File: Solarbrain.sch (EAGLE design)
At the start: 50 parts, among them IC1 MCP73871, Q1 MOSFET-NCHANNELSMD, Q2 MOSFET-NCHANNELFDD8580, Q3 MOSFET-NCHANNELSMD, U1 ATMEGA128_SMD

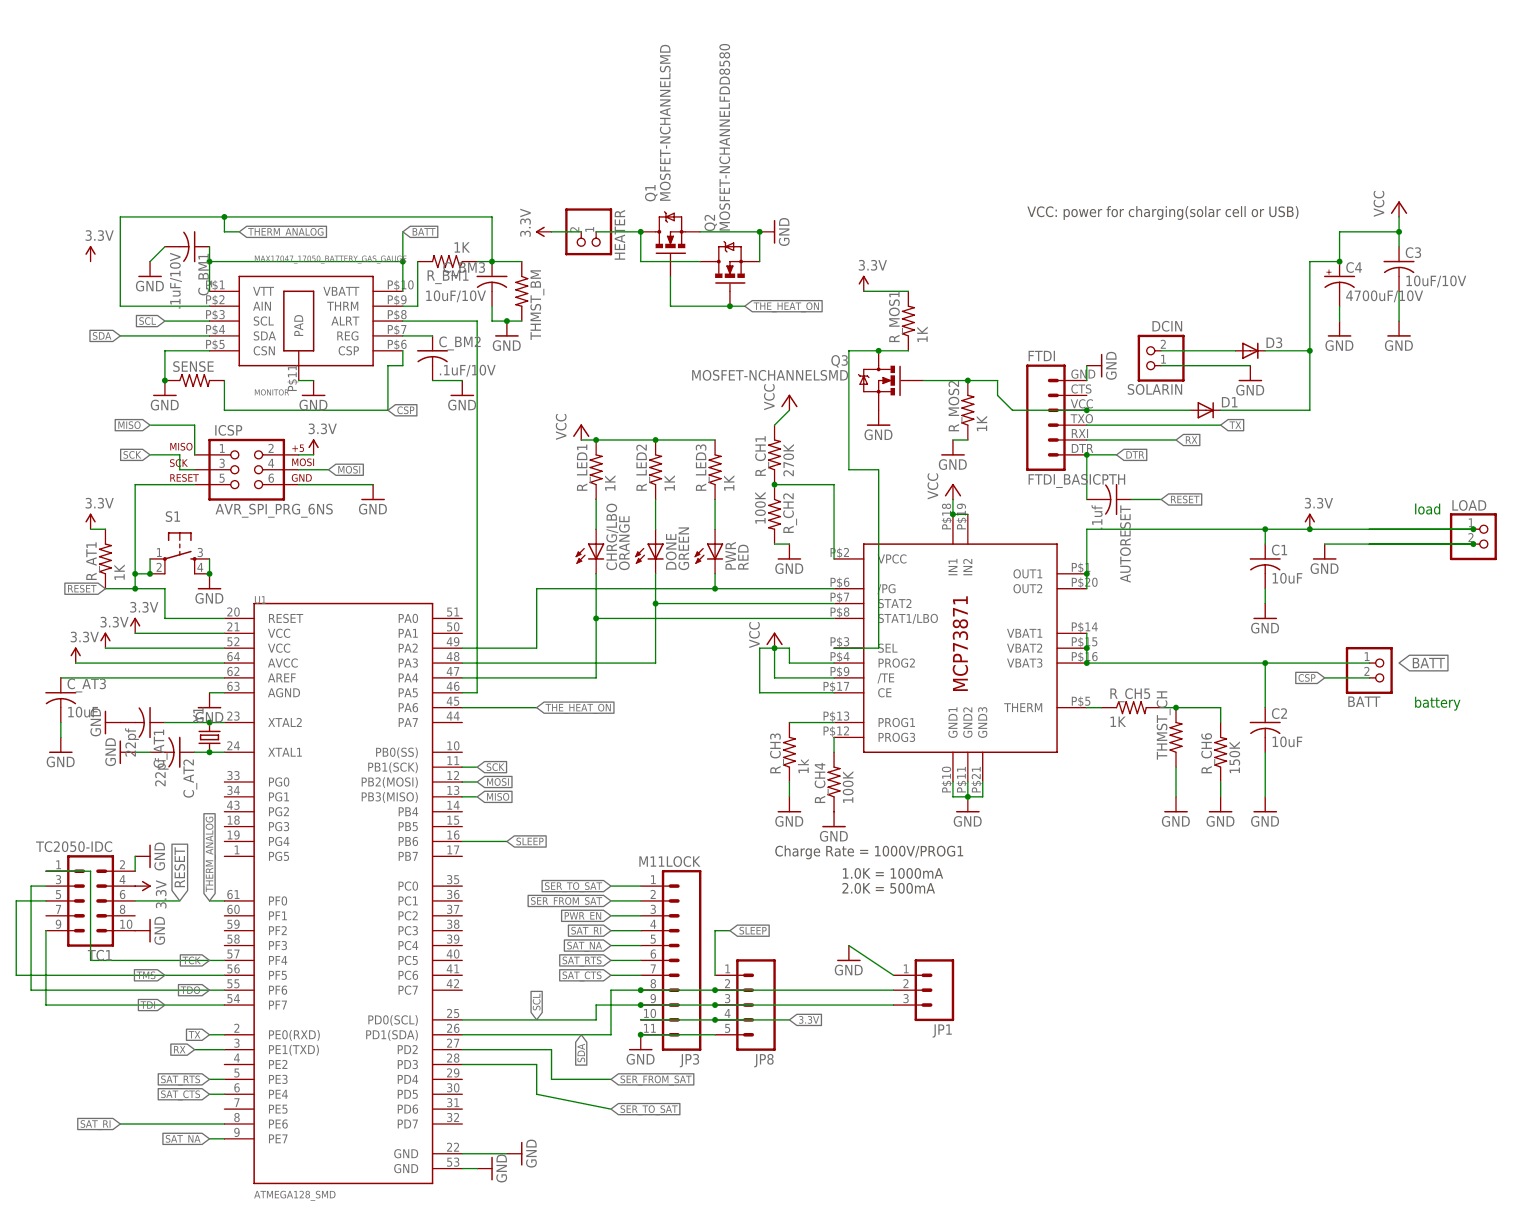
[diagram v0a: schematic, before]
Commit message: fixed a broken connection, clarification on schematic
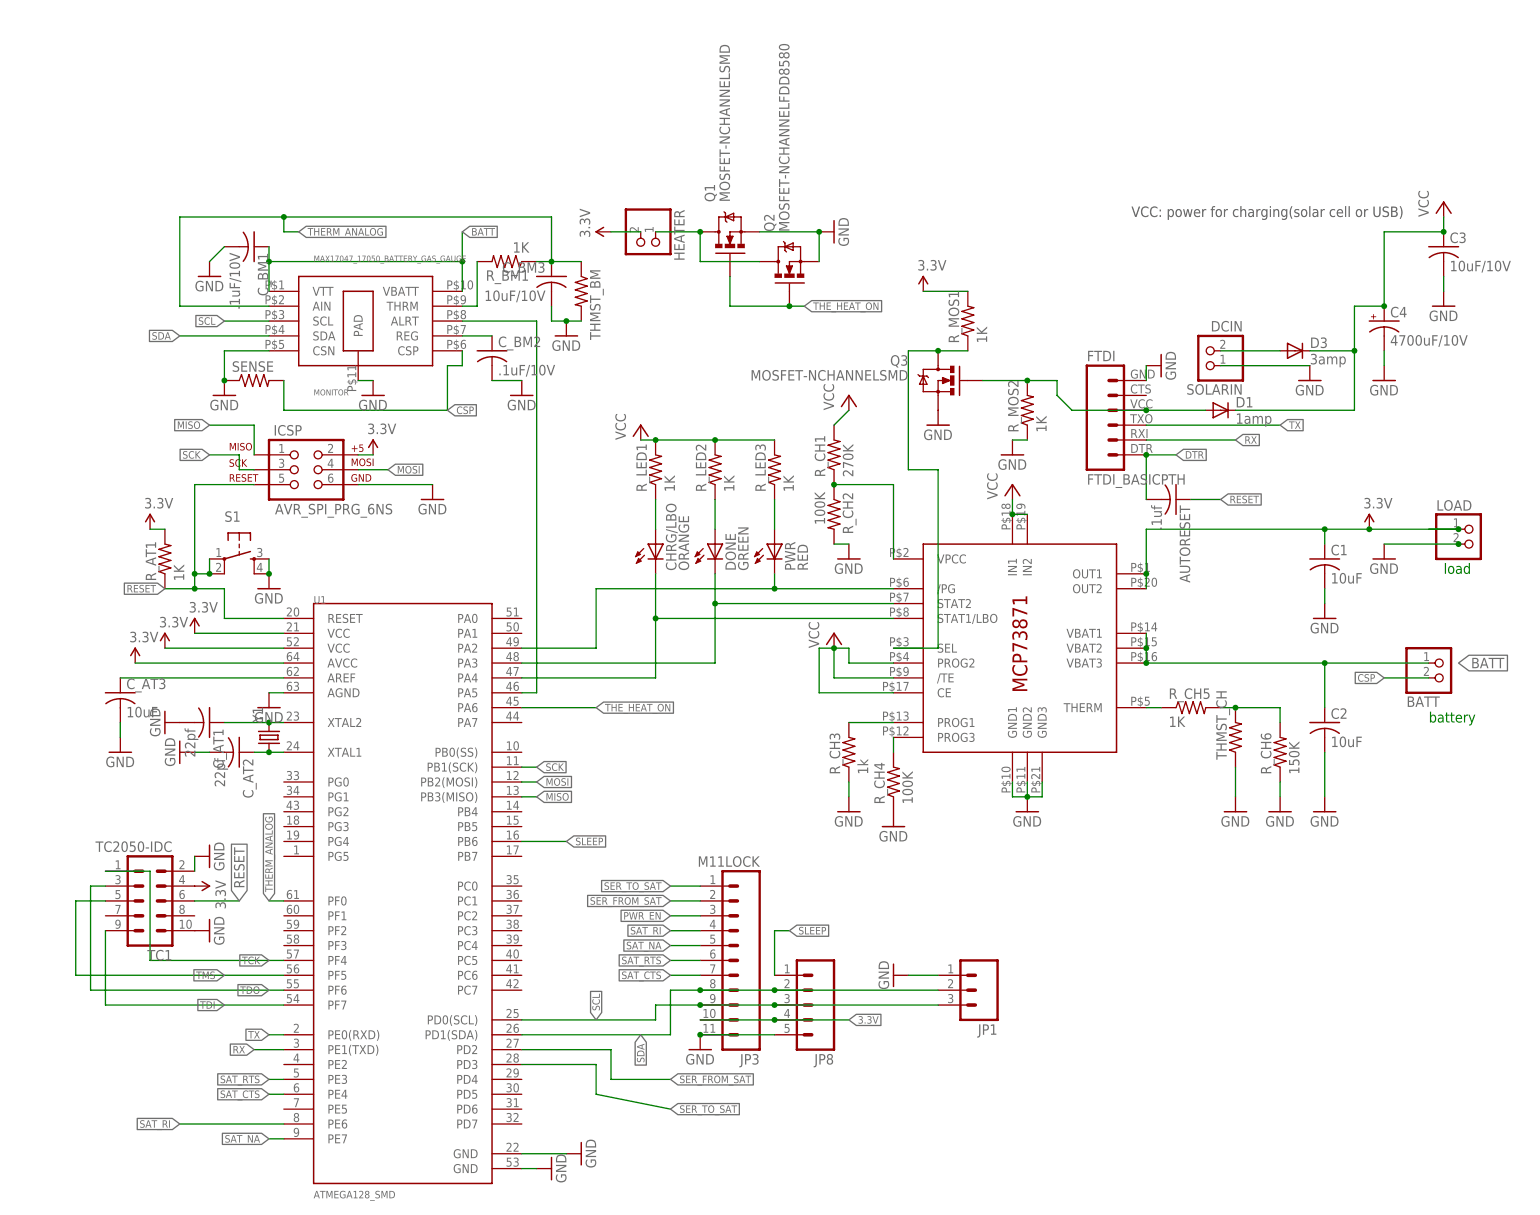
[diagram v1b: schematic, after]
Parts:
- D1: value (none) -> 1amp
- D3: value (none) -> 3amp
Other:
- note removed: "1.0K = 1000mA"
- note removed: "2.0K = 500mA"
- note removed: "Charge Rate = 1000V/PROG1"
- moved on the sheet: AUTORESET, BATT, C1, C2, C3, C4, CHRG/LBO, C_AT1, C_AT2, C_AT3, C_BM1, C_BM2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
